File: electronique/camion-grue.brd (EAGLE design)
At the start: 129 x 106 mm, 131 parts, among them P1 RGEF800, Q1 BSS138, Q2 BSS138, U1 TEENSY_3.5_DIL+USB, U2 TEENSY_3.1-3.2_DIL

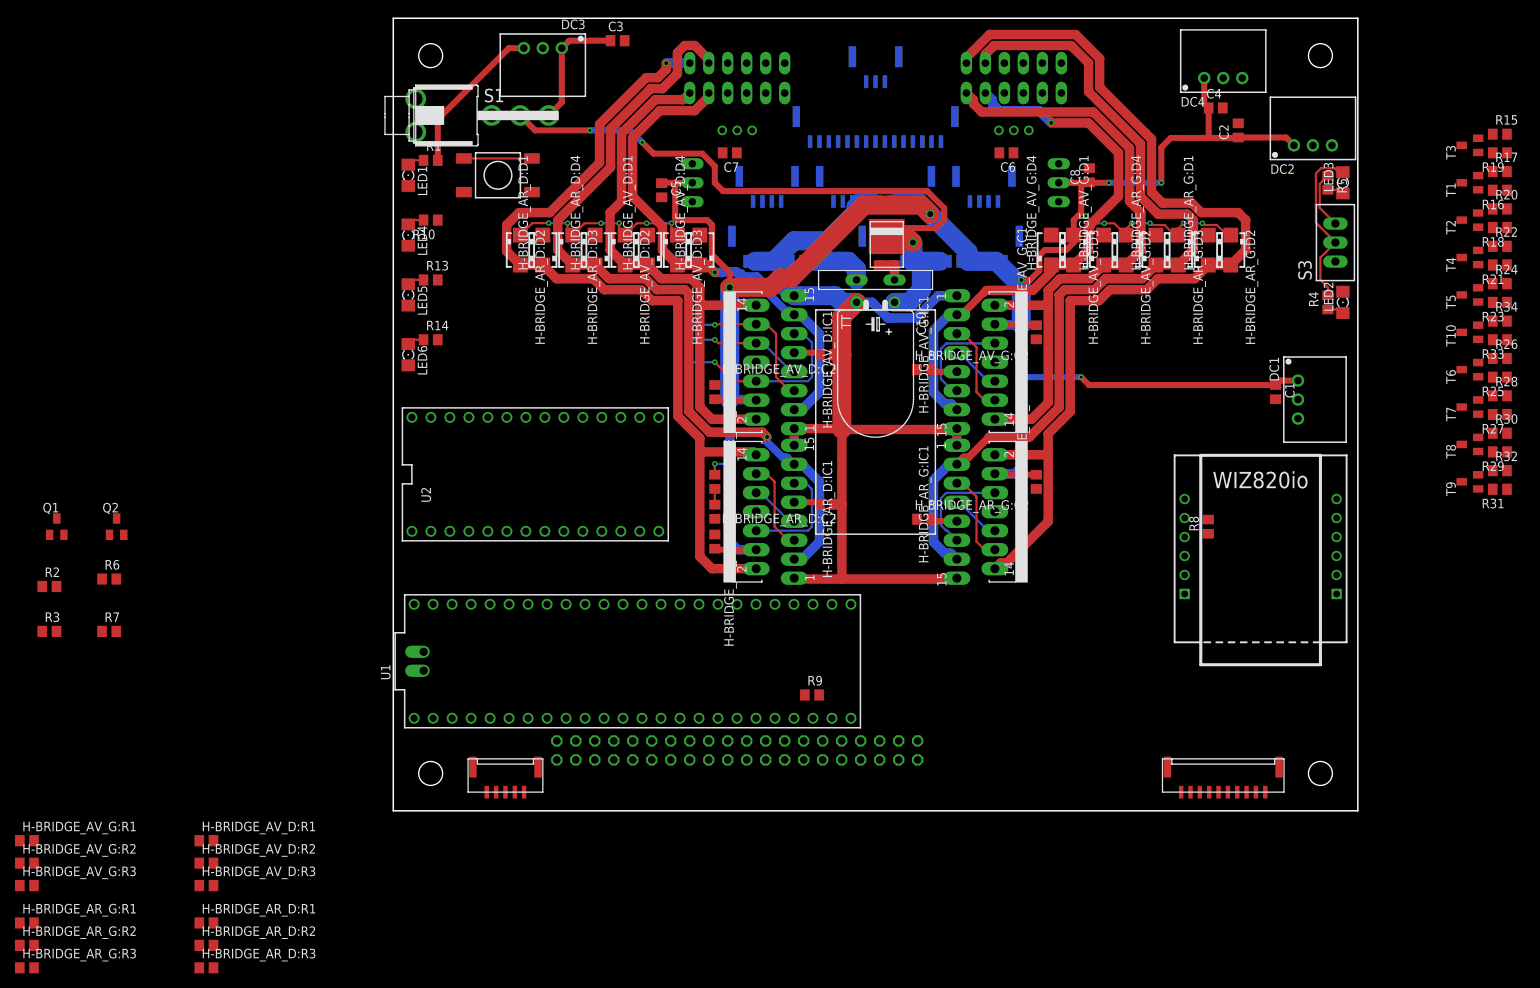
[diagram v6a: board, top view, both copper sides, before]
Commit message: Elec: routage catre principale presque fini !
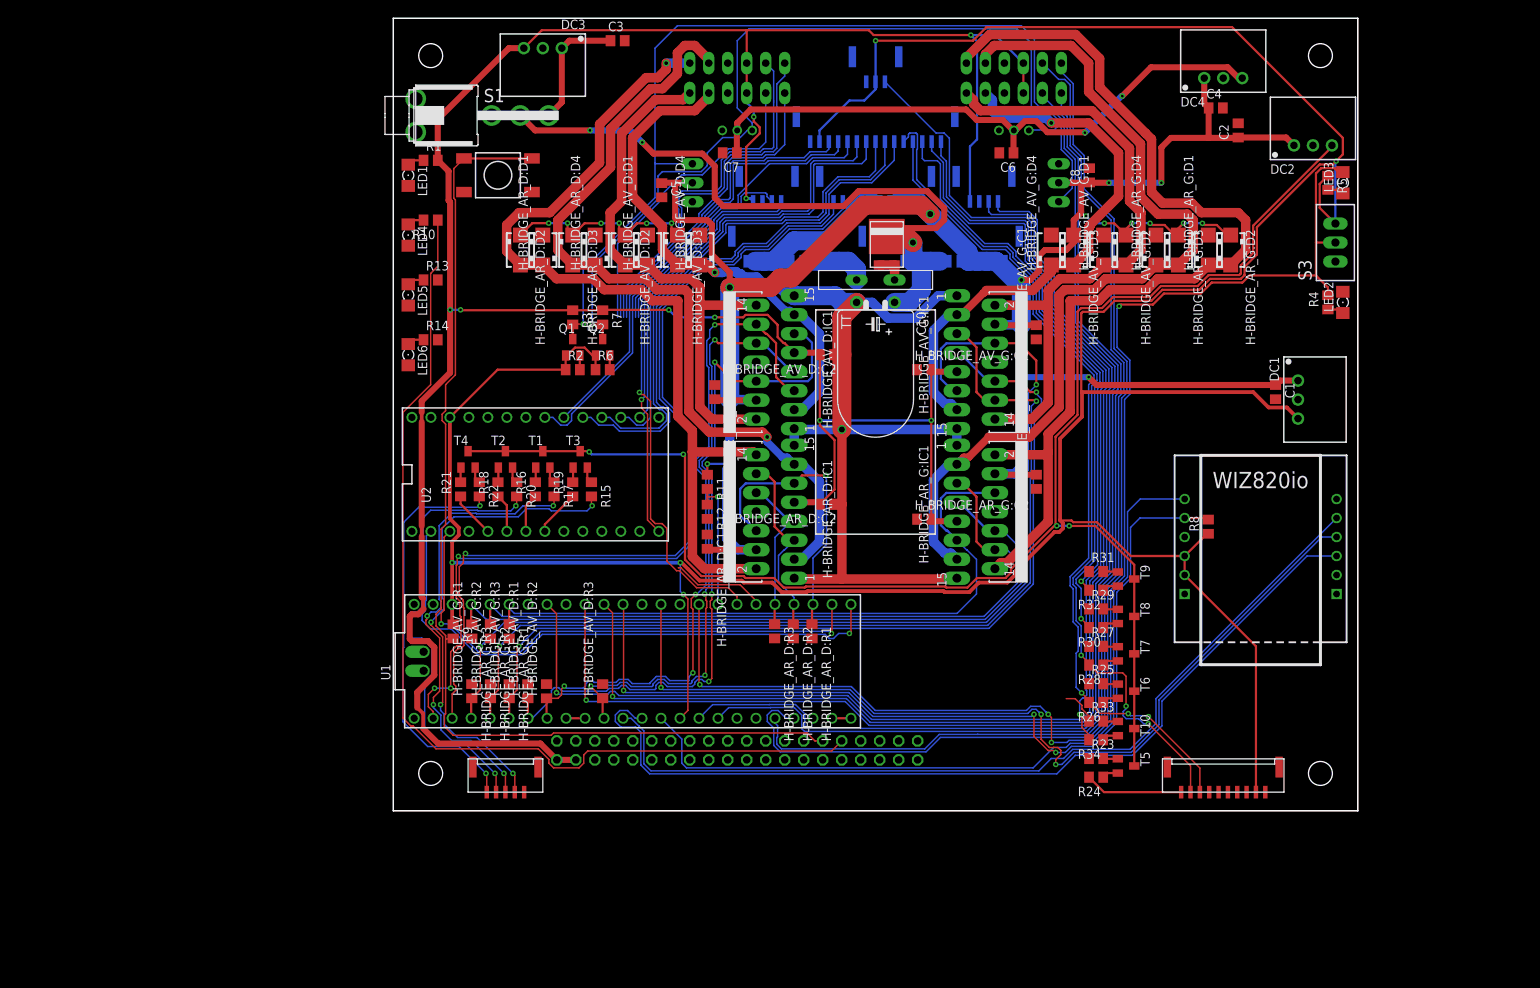
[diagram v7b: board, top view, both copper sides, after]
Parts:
- moved R21 142.2 mm to (9.00, 43.0), turned to 90 degrees
- moved R22 140.3 mm to (11.5, 43.0), turned to 270 degrees
- moved R18 138.5 mm to (14.0, 43.0), turned to 90 degrees
- moved R20 136.7 mm to (16.5, 43.0), turned to 270 degrees
- moved T4 136.7 mm to (10.0, 47.0), turned to 0 degrees
- moved R16 135.1 mm to (19.0, 43.0), turned to 90 degrees
- moved R17 133.4 mm to (21.5, 43.0), turned to 270 degrees
- moved T2 132.9 mm to (15.0, 47.0), turned to 0 degrees
- moved R19 131.9 mm to (24.0, 43.0), turned to 90 degrees
- moved R15 130.5 mm to (26.5, 43.0), turned to 270 degrees
- moved T1 129.4 mm to (20.0, 47.0), turned to 0 degrees
- moved T3 126.2 mm to (25.0, 47.0), turned to 0 degrees
- moved H-BRIDGE_AR_D:R1 89.9 mm to (56.0, 24.0), turned to 270 degrees
- moved H-BRIDGE_AR_D:R2 89.0 mm to (53.5, 24.0), turned to 270 degrees
- moved H-BRIDGE_AR_D:R3 88.3 mm to (51.0, 24.0), turned to 270 degrees
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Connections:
- removed net VIN: U1.VIN, U2.VIN
- new net VIN1[NC]: U1.VIN
- new net VIN2[NC]: U2.VIN
- net DEL_GYRO_1_PWM: now also U2.6; no longer U2.3
- net DEL_GYRO_2_PWM: now also U2.5; no longer U2.4
- net DEL_GYRO_3_PWM: now also U2.4; no longer U2.5
- net DEL_GYRO_4_PWM: now also U2.3; no longer U2.6
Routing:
- net +3V3: track 7.74 -> 435.5 mm, vias 0 -> 5
- net +5V: track 35.1 -> 368.9 mm, vias 0 -> 9
- net +3V3_LEDS: track 0.00 -> 213.6 mm, vias 0 -> 4
- net JUMPER: track 0.00 -> 188.5 mm, vias 0 -> 1
- net ENC_G_B: track 0.00 -> 161.4 mm, vias 0 -> 1
- net CHOOSE_COLOR: track 22.7 -> 181.6 mm, vias 0 -> 4
- net ENC_G_A: track 0.00 -> 158.1 mm, vias 0 -> 1
- net ENC_AR_G_B: track 0.00 -> 147.9 mm
- net ENC_AV_G_A: track 0.00 -> 145.8 mm
- net ENC_AR_G_A: track 0.00 -> 143.1 mm
- net ENC_AV_G_B: track 0.00 -> 142.9 mm
- net N$5: track 0.00 -> 132.4 mm
- net N$2: track 9.10 -> 140.4 mm
- net SERIAL_AX12_5V: track 0.00 -> 127.4 mm, vias 0 -> 1
- net ETH_SCLK: track 0.00 -> 124.8 mm, vias 0 -> 3
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
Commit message: Elec cockpit terminée
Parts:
- added USB_BACKUP_DEBUG: (no value), pinhead:1X03
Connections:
- new net USB_D+: U1.USBD+, USB_BACKUP_DEBUG.2
- new net USB_D-: U1.USBD-, USB_BACKUP_DEBUG.3
- net GND: now also USB_BACKUP_DEBUG.1
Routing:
- net USB_D+: track 0.00 -> 155.3 mm
- net USB_D-: track 0.00 -> 149.6 mm
- net SDA: track 59.0 -> 208.1 mm, vias 0 -> 4
- net SCL: track 64.3 -> 212.2 mm, vias 0 -> 4
- net TOF_AV_G: track 0.00 -> 135.3 mm, vias 0 -> 5
- net TOF_AV: track 0.00 -> 120.1 mm, vias 0 -> 5
- net TOF_AV_D: track 0.00 -> 115.3 mm, vias 0 -> 5
- net DEL_FEUX_RECUL_PWM: track 4.97 -> 117.5 mm, vias 0 -> 2
- net DEL_FEUX_STOP_PWM: track 0.00 -> 109.9 mm, vias 0 -> 2
- net DEL_FEUX_NUIT_AR_PWM: track 0.00 -> 107.9 mm, vias 0 -> 2
- net DEL_CLIGNOTANT_D_PWM: track 0.00 -> 106.0 mm, vias 0 -> 2
- net DEL_FEUX_NUIT_AV_PWM: track 0.00 -> 93.5 mm, vias 0 -> 3
- net SERIAL_XL320: track 4.44 -> 88.3 mm
- net DEL_CLIGNOTANT_G_PWM: track 0.00 -> 81.1 mm, vias 0 -> 3
- net ENC_AR_D_A: track 49.0 -> 129.7 mm, vias 0 -> 3
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- added copper zone on layer 1, net GND
- added copper zone on layer 16, net GND
